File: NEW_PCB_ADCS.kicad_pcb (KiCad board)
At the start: 2 copper layers, 42 x 42 mm, 73 parts, among them IC1 DRV8212DSGR, IC2 DRV8212DSGR, IC3 DRV8212DSGR, J1 SWD, J2 PANEL1, J3 PANEL2, J4 PANEL3, J5 PANEL4, J6 MTQZ, J7 Micro_SD_Card_Det_Hirose_DM3AT, J8 PQ9-Connector, U1 AD8603, U2 47K, U3 STM32L476RGTx, U4 TCAN334, U5 LIS3MDL, U6 BNO055, Y1 Crystal

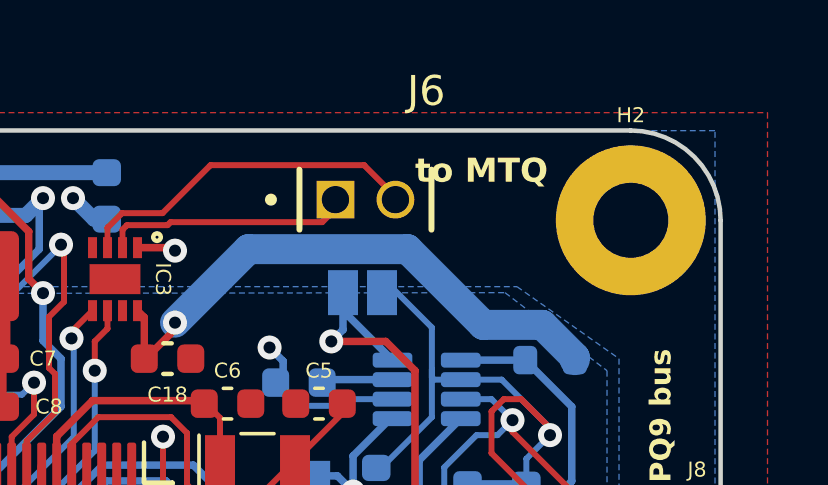
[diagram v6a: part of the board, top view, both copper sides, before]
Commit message: Remove paste from connectors, relink GND mounting pins
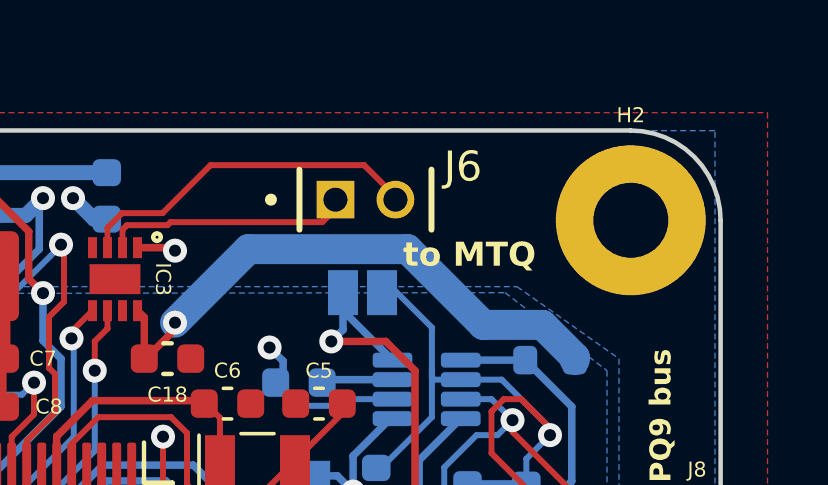
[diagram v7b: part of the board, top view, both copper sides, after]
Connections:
- J2 pad MP: (no net) -> GND
- J3 pad MP: (no net) -> GND
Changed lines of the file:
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@@
     (pad "4" smd roundrect (at 1.875 -1.25 90) (size 0.8 1.3) (layers "F.Cu" "F.Paste" "F.Mask") (roundrect_rratio 0.25)
       (net 20 "/Connectors/LIGHT_2") (pinfunction "Pin_4") (pintype "passive"))
-    (pad "MP" smd roundrect (at -4.425 1.5 90) (size 2.1 3) (layers "F.Cu" "F.Paste" "F.Mask") (roundrect_rratio 0.1190480952))
-    (pad "MP" smd roundrect (at 4.425 1.5 90) (size 2.1 3) (layers "F.Cu" "F.Paste" "F.Mask") (roundrect_rratio 0.1190480952))
+    (pad "MP" smd roundrect (at -4.425 1.5 90) (size 2.1 3) (layers "F.Cu" "F.Paste" "F.Mask") (roundrect_rratio 0.1190480952)
+      (net 4 "GND"))
+    (pad "MP" smd roundrect (at 4.425 1.5 90) (size 2.1 3) (layers "F.Cu" "F.Paste" "F.Mask") (roundrect_rratio 0.1190480952)
+      (net 4 "GND"))
     (model "${KICAD6_3DMODEL_DIR}/Connector_Molex.3dshapes/Molex_PicoBlade_53398-0471_1x04-1MP_P1.25mm_Vertical.wrl"
       (offset (xyz 0 0 0))
@@
       (net 17 "/Connectors/LIGHT_1") (pinfunction "Pin_4") (pintype "passive"))
     (pad "MP" smd roundrect (at -4.425 1.5) (size 2.1 3) (layers "F.Cu" "F.Paste" "F.Mask") (roundrect_rratio 0.1190480952))
-    (pad "MP" smd roundrect (at 4.425 1.5) (size 2.1 3) (layers "F.Cu" "F.Paste" "F.Mask") (roundrect_rratio 0.1190480952))
+    (pad "MP" smd roundrect (at 4.425 1.5) (size 2.1 3) (layers "F.Cu" "F.Paste" "F.Mask") (roundrect_rratio 0.1190480952)
+      (net 4 "GND"))
     (model "${KICAD6_3DMODEL_DIR}/Connector_Molex.3dshapes/Molex_PicoBlade_53398-0471_1x04-1MP_P1.25mm_Vertical.wrl"
       (offset (xyz 0 0 0))
@@
     (property "SnapEDA_Link" "https://www.snapeda.com/parts/SQT-102-03-F-S/Samtec/view-part/?ref=snap")
     (attr through_hole)
-    (fp_text reference "J6" (at 3.025 -3.62) (layer "F.SilkS")
+    (fp_text reference "J6" (at 4.2523 -1.1) (layer "F.SilkS")
         (effects (font (size 1 1) (thickness 0.15)))
     )
@@
         (effects (font (size 1 1) (thickness 0.15)))
     )
-    (fp_poly
-      (pts
-        (xy 0.85 0.85)
-        (xy 0.85 -0.85)
-        (xy 0.385 -0.85)
-        (xy 0.378 -0.85)
-        (xy 0.371 -0.851)
-        (xy 0.365 -0.852)
-        (xy 0.358 -0.853)
-        (xy 0.351 -0.854)
-        (xy 0.345 -0.856)
-        (xy 0.338 -0.859)
-        (xy 0.332 -0.861)
-        (xy 0.326 -0.864)
-        (xy 0.32 -0.867)
-        (xy 0.314 -0.871)
-        (xy 0.309 -0.875)
-        (xy 0.303 -0.879)
-        (xy 0.298 -0.883)
-        (xy 0.293 -0.888)
-        (xy 0.288 -0.893)
-        (xy 0.284 -0.898)
-        (xy 0.28 -0.904)
-        (xy 0.276 -0.909)
-        (xy 0.272 -0.915)
-        (xy 0.269 -0.921)
-        (xy 0.266 -0.927)
-        (xy 0.264 -0.933)
-        (xy 0.261 -0.94)
-        (xy 0.259 -0.946)
-        (xy 0.258 -0.953)
-        (xy 0.257 -0.96)
-        (xy 0.256 -0.966)
-        (xy 0.255 -0.973)
-        (xy 0.255 -0.98)
-        (xy 0.255 -1.97)
-        (xy -0.255 -1.97)
-        (xy -0.255 -0.98)
-        (xy -0.255 -0.973)
-        (xy -0.256 -0.966)
-        (xy -0.257 -0.96)
-        (xy -0.258 -0.953)
-        (xy -0.259 -0.946)
-        (xy -0.261 -0.94)
-        (xy -0.264 -0.933)
-        (xy -0.266 -0.927)
-        (xy -0.269 -0.921)
-        (xy -0.272 -0.915)
-        (xy -0.276 -0.909)
-        (xy -0.28 -0.904)
-        (xy -0.284 -0.898)
-        (xy -0.288 -0.893)
-        (xy -0.293 -0.888)
-        (xy -0.298 -0.883)
-        (xy -0.303 -0.879)
-        (xy -0.309 -0.875)
-        (xy -0.314 -0.871)
-        (xy -0.32 -0.867)
-        (xy -0.326 -0.864)
-        (xy -0.332 -0.861)
-        (xy -0.338 -0.859)
-        (xy -0.345 -0.856)
-        (xy -0.351 -0.854)
-        (xy -0.358 -0.853)
-        (xy -0.365 -0.852)
-        (xy -0.371 -0.851)
-        (xy -0.378 -0.85)
-        (xy -0.385 -0.85)
-        (xy -0.85 -0.85)
-        (xy -0.85 0.85)
-        (xy 0.85 0.85)
-      )
-      (stroke (width 0.01) (type solid)) (fill solid) (layer "F.Paste"))
-    (fp_poly
-      (pts
-        (xy 1.15 -0.85)
-        (xy 1.15 0.85)
-        (xy 1.615 0.85)
-        (xy 1.622 0.85)
-        (xy 1.629 0.851)
-        (xy 1.635 0.852)
-        (xy 1.642 0.853)
-        (xy 1.649 0.854)
-        (xy 1.655 0.856)
-        (xy 1.662 0.859)
-        (xy 1.668 0.861)
-        (xy 1.674 0.864)
-        (xy 1.68 0.867)
-        (xy 1.686 0.871)
-        (xy 1.691 0.875)
-        (xy 1.697 0.879)
-        (xy 1.702 0.883)
-        (xy 1.707 0.888)
-        (xy 1.712 0.893)
-        (xy 1.716 0.898)
-        (xy 1.72 0.904)
-        (xy 1.724 0.909)
-        (xy 1.728 0.915)
-        (xy 1.731 0.921)
-        (xy 1.734 0.927)
-        (xy 1.736 0.933)
-        (xy 1.739 0.94)
-        (xy 1.741 0.946)
-        (xy 1.742 0.953)
-        (xy 1.743 0.96)
-        (xy 1.744 0.966)
-        (xy 1.745 0.973)
-        (xy 1.745 0.98)
-        (xy 1.745 1.97)
-        (xy 2.255 1.97)
-        (xy 2.255 0.98)
-        (xy 2.255 0.973)
-        (xy 2.256 0.966)
-        (xy 2.257 0.96)
-        (xy 2.258 0.953)
-        (xy 2.259 0.946)
-        (xy 2.261 0.94)
-        (xy 2.264 0.933)
-        (xy 2.266 0.927)
-        (xy 2.269 0.921)
-        (xy 2.272 0.915)
-        (xy 2.276 0.909)
-        (xy 2.28 0.904)
-        (xy 2.284 0.898)
-        (xy 2.288 0.893)
-        (xy 2.293 0.888)
-        (xy 2.298 0.883)
-        (xy 2.303 0.879)
-        (xy 2.309 0.875)
-        (xy 2.314 0.871)
-        (xy 2.32 0.867)
-        (xy 2.326 0.864)
-        (xy 2.332 0.861)
-        (xy 2.338 0.859)
-        (xy 2.345 0.856)
-        (xy 2.351 0.854)
-        (xy 2.358 0.853)
-        (xy 2.365 0.852)
-        (xy 2.371 0.851)
-        (xy 2.378 0.85)
-        (xy 2.385 0.85)
-        (xy 2.85 0.85)
-        (xy 2.85 -0.85)
-        (xy 1.15 -0.85)
-      )
-      (stroke (width 0.01) (type solid)) (fill solid) (layer "F.Paste"))
     (fp_line (start -1.2 -1) (end -1.2 1)
       (stroke (width 0.2) (type solid)) (layer "F.SilkS"))
@@
     (fp_circle (center -2.15 0) (end -2.05 0)
       (stroke (width 0.2) (type solid)) (fill none) (layer "F.Fab"))
-    (pad "01" thru_hole rect (at 0 0) (size 1.26 1.26) (drill 0.91) (layers "*.Cu" "*.Mask")
+    (pad "01" thru_hole rect (at 0 0) (size 1.26 1.26) (drill 0.8) (layers "*.Cu" "*.Mask")
       (net 23 "/Connectors/MQT3+") (pinfunction "01") (pintype "passive") (solder_mask_margin 0.102))
-    (pad "02" thru_hole circle (at 2 0) (size 1.26 1.26) (drill 0.91) (layers "*.Cu" "*.Mask")
+    (pad "02" thru_hole circle (at 2 0) (size 1.26 1.26) (drill 0.8) (layers "*.Cu" "*.Mask")
       (net 24 "/Connectors/MQT3-") (pinfunction "02") (pintype "passive") (solder_mask_margin 0.102))
   )
@@
     (effects (font (size 0.8 0.8) (thickness 0.1) bold) (justify left bottom))
   )
-  (gr_text "to MTQ" (at 205 50.4) (layer "F.SilkS")
+  (gr_text "to MTQ" (at 204.6 53.2) (layer "F.SilkS")
     (effects (font (size 0.8 0.8) (thickness 0.1) bold) (justify left bottom))
   )
@@
   (segment (start 195.234314 51.35) (end 196.584314 51.35) (width 0.2) (layer "F.Cu") (net 24))
   (segment (start 198.184314 49.75) (end 203.3043 49.75) (width 0.2) (layer "F.Cu") (net 24))
-  (segment (start 204.378306 50.9712) (end 204.6525 50.9712) (width 0.2) (layer "F.Cu") (net 24))
   (segment (start 194.75 52.5) (end 194.75 51.834314) (width 0.2) (layer "F.Cu") (net 24))
   (segment (start 197.481 68.195) (end 198.321685 68.195) (width 0.25) (layer "F.Cu") (net 25))

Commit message: Oops...forgot to save
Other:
- board text added: "Designed by Niki Sajjad, Konstantinos Kanavouras"
- board text removed: "Designed by Niki Sajjad"
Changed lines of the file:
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@@
     (effects (font (size 0.5 0.5) (thickness 0.1) bold) (justify left bottom))
   )
-  (gr_text "Designed by\nNiki Sajjad" (at 194.4 79.2) (layer "F.SilkS")
+  (gr_text "Designed by\nNiki Sajjad, Konstantinos Kanavouras" (at 194.4 79.2) (layer "F.SilkS")
     (effects (font (size 0.5 0.5) (thickness 0.1) bold) (justify bottom))
   )
